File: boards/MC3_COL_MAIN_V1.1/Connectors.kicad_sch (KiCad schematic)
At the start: 11 parts, among them J13 HARNESS_FFC_6P, J3 ENC_leaf1, J4 ENC_leaf2, J5 ENC_leaf3, J6 ENC_leaf4

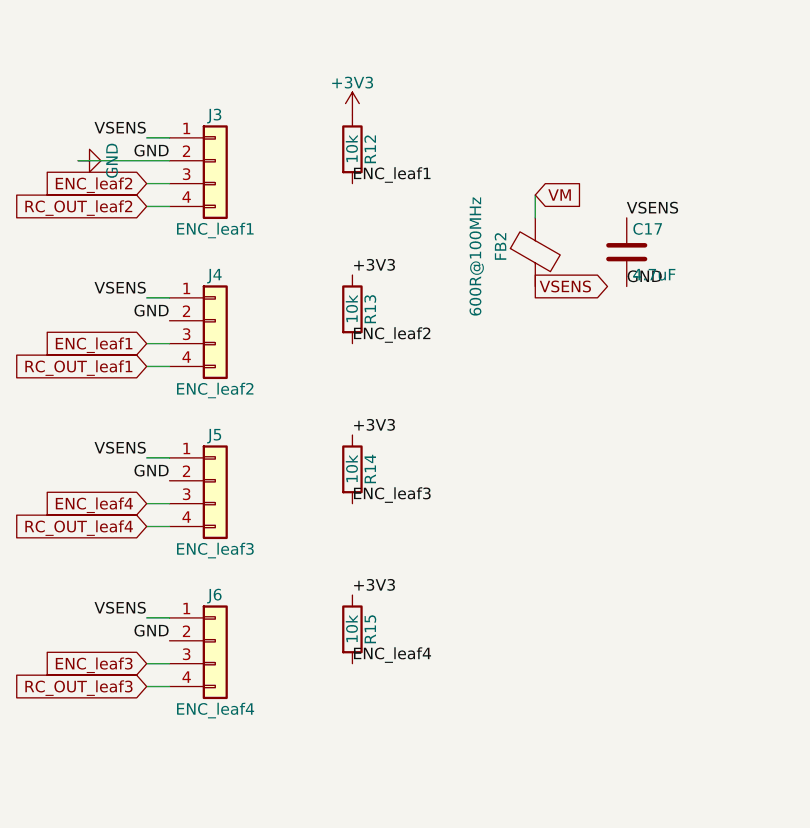
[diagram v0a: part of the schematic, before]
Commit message: V1.1: ENC pull-up islands remapped with the connector swap (R12=leaf2, R13=leaf1, R14=leaf4, R15=leaf3)
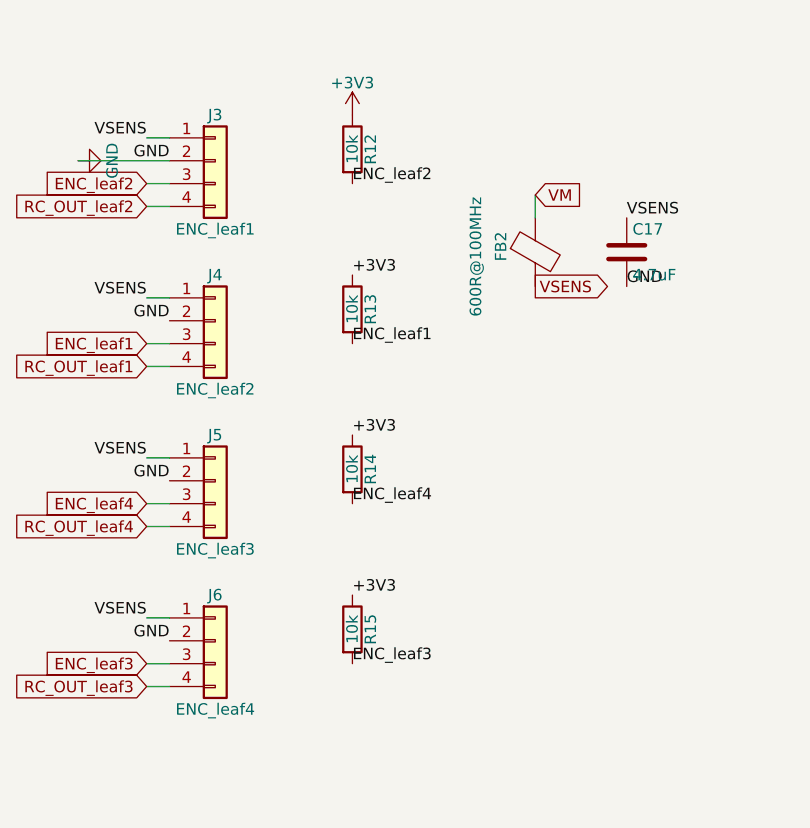
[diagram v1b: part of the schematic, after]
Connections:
- net ENC_leaf1: now also R13.2; no longer R12.2
- net ENC_leaf2: now also R12.2; no longer R13.2
- net ENC_leaf3: now also R15.2; no longer R14.2
- net ENC_leaf4: now also R14.2; no longer R15.2
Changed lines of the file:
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@@
-		)
-	)
-	(label "ENC_leaf2"
-		(at 74.93 69.85 0)
-		(effects
-			(font
-				(size 1.27 1.27)
-			)
-			(justify left bottom)
 		)
 	)
@@
 		)
 	)
-	(label "ENC_leaf4"
-		(at 74.93 105.41 0)
-		(effects
-			(font
-				(size 1.27 1.27)
-			)
-			(justify left bottom)
-		)
-	)
 	(label "+3V3"
 		(at 74.93 62.23 0)
-		(effects
-			(font
-				(size 1.27 1.27)
-			)
-			(justify left bottom)
-		)
-	)
-	(label "ENC_leaf1"
-		(at 74.93 52.07 0)
-		(effects
-			(font
-				(size 1.27 1.27)
-			)
-			(justify left bottom)
-		)
-	)
-	(label "ENC_leaf3"
-		(at 74.93 87.63 0)
 		(effects
 			(font
@@
 		(effects
 			(font
+				(size 1.27 1.27)
+			)
+			(justify left bottom)
+		)
+	)
+	(label "ENC_leaf2"
+		(at 74.93 52.07 0)
+		(effects
+			(font
+				(size 1.27 1.27)
+			)
+			(justify left bottom)
+		)
+	)
+	(label "ENC_leaf1"
+		(at 74.93 69.85 0)
+		(effects
+			(font
+				(size 1.27 1.27)
+			)
+			(justify left bottom)
+		)
+	)
+	(label "ENC_leaf4"
+		(at 74.93 87.63 0)
+		(effects
+			(font
+				(size 1.27 1.27)
+			)
+			(justify left bottom)
+		)
+	)
+	(label "ENC_leaf3"
+		(at 74.93 105.41 0)
+		(effects
+			(font
